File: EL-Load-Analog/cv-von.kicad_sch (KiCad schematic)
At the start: 35 parts, among them Q3 MMBT5551, Q5 MMBT5401, Q6 MMBT5551, U401 AD8038, U402 LM393, U403 74HCT02

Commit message: Working on #4,#2 fixed #8,#22
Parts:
- C401: value 670n -> 680n; Part Name (none) -> C_680nF_25V_X7R_10%_0805
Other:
- note added: "TODO: Select different opamp. TLV2370 (pin compatible)"
- note removed: "TODO: Select different opamp."
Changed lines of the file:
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@@
     (effects (font (size 1.27 1.27)) (justify left bottom))
   )
-  (text "TODO: Select different opamp." (at 108.585 157.48 0)
+  (text "TODO: Select different opamp.\nTLV2370 (pin compatible)\n"
+    (at 108.585 157.48 0)
     (effects (font (size 1.27 1.27)) (justify left bottom))
   )
@@
   (symbol (lib_id "Device:C_Small") (at 102.87 191.135 90) (unit 1)
     (in_bom yes) (on_board yes) (dnp no) (fields_autoplaced)
-    (property "Reference" "C401" (at 102.8763 184.785 90)
-      (effects (font (size 1.27 1.27)))
-    )
-    (property "Value" "670n" (at 102.8763 187.325 90)
+    (property "Reference" "C401" (at 102.8763 184.15 90)
+      (effects (font (size 1.27 1.27)))
+    )
+    (property "Value" "680n" (at 102.8763 186.69 90)
       (effects (font (size 1.27 1.27)))
     )
@@
       (effects (font (size 1.27 1.27)) hide)
     )
+    (property "Part Name" "C_680nF_25V_X7R_10%_0805" (at 102.87 191.135 0)
+      (effects (font (size 1.27 1.27)) hide)
+    )

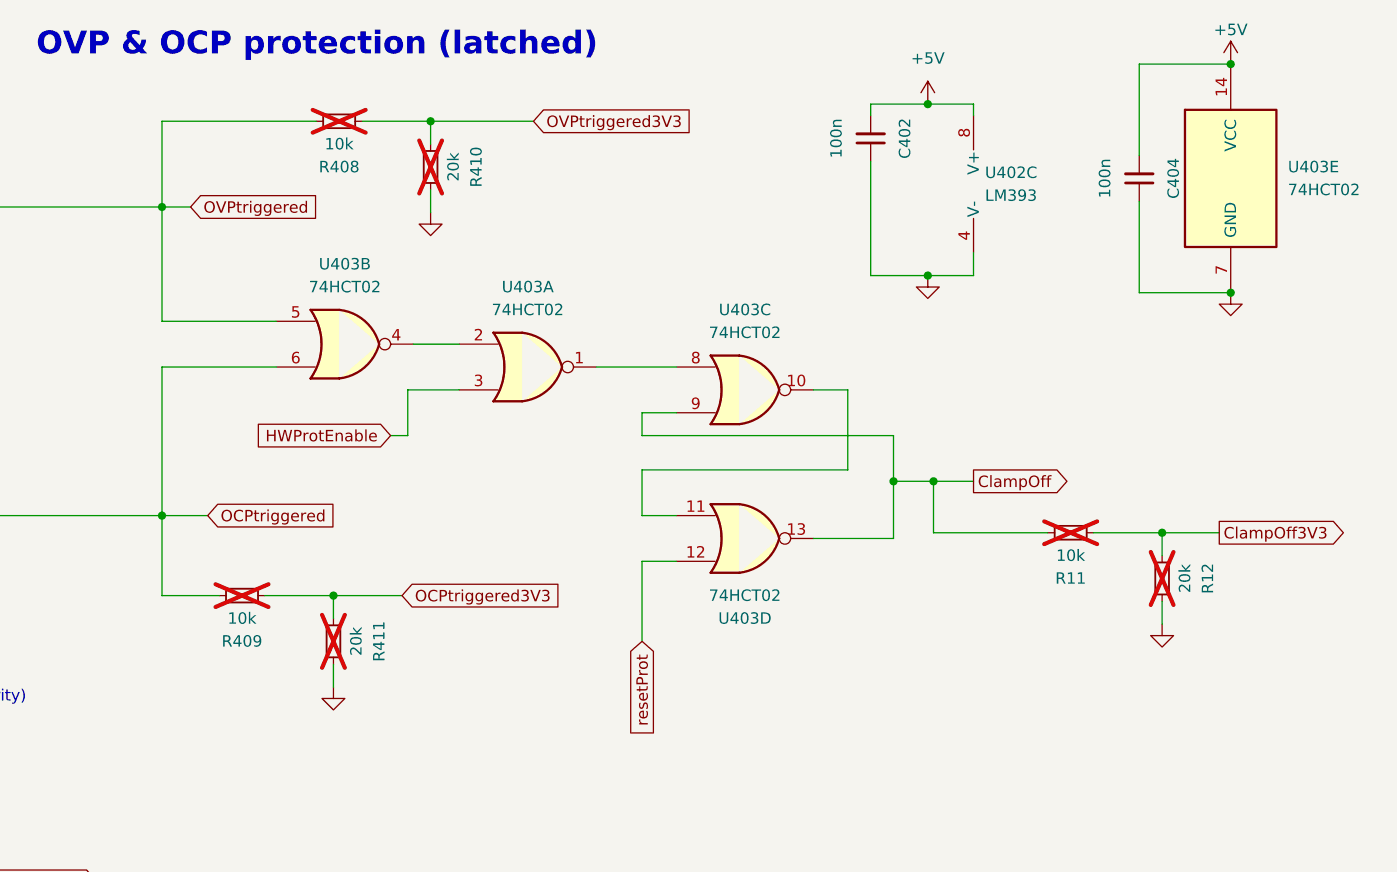
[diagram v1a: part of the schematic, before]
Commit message: Fixing issues from #4, adding ESD protection (#6)
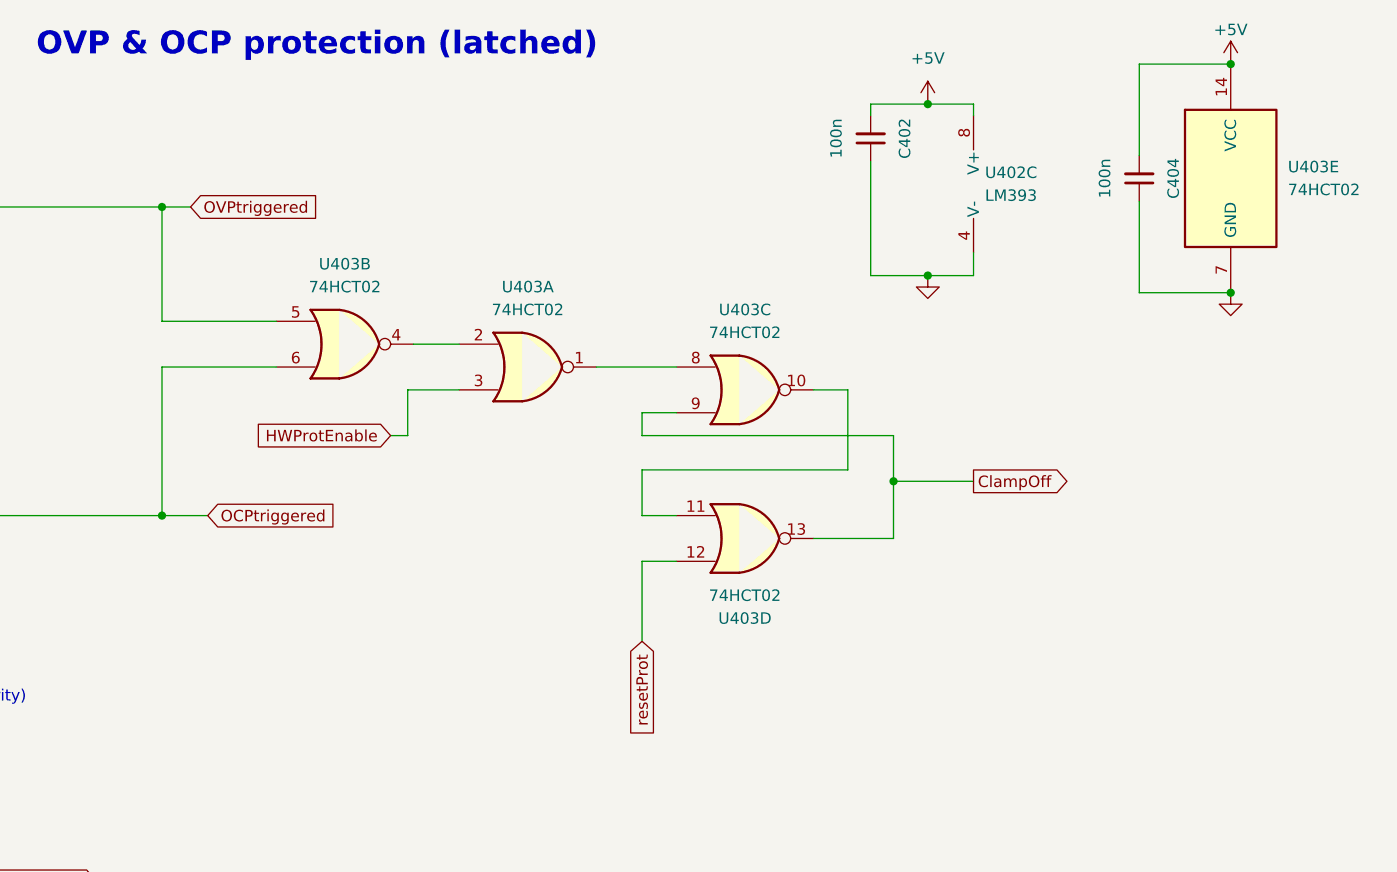
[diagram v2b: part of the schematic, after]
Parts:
- removed R11, R408, R409: 10k, Resistor_SMD:R_0805_2012Metric, symbol Device:R_Small
- removed R12, R410, R411: 20k, Resistor_SMD:R_0805_2012Metric, symbol Device:R_Small

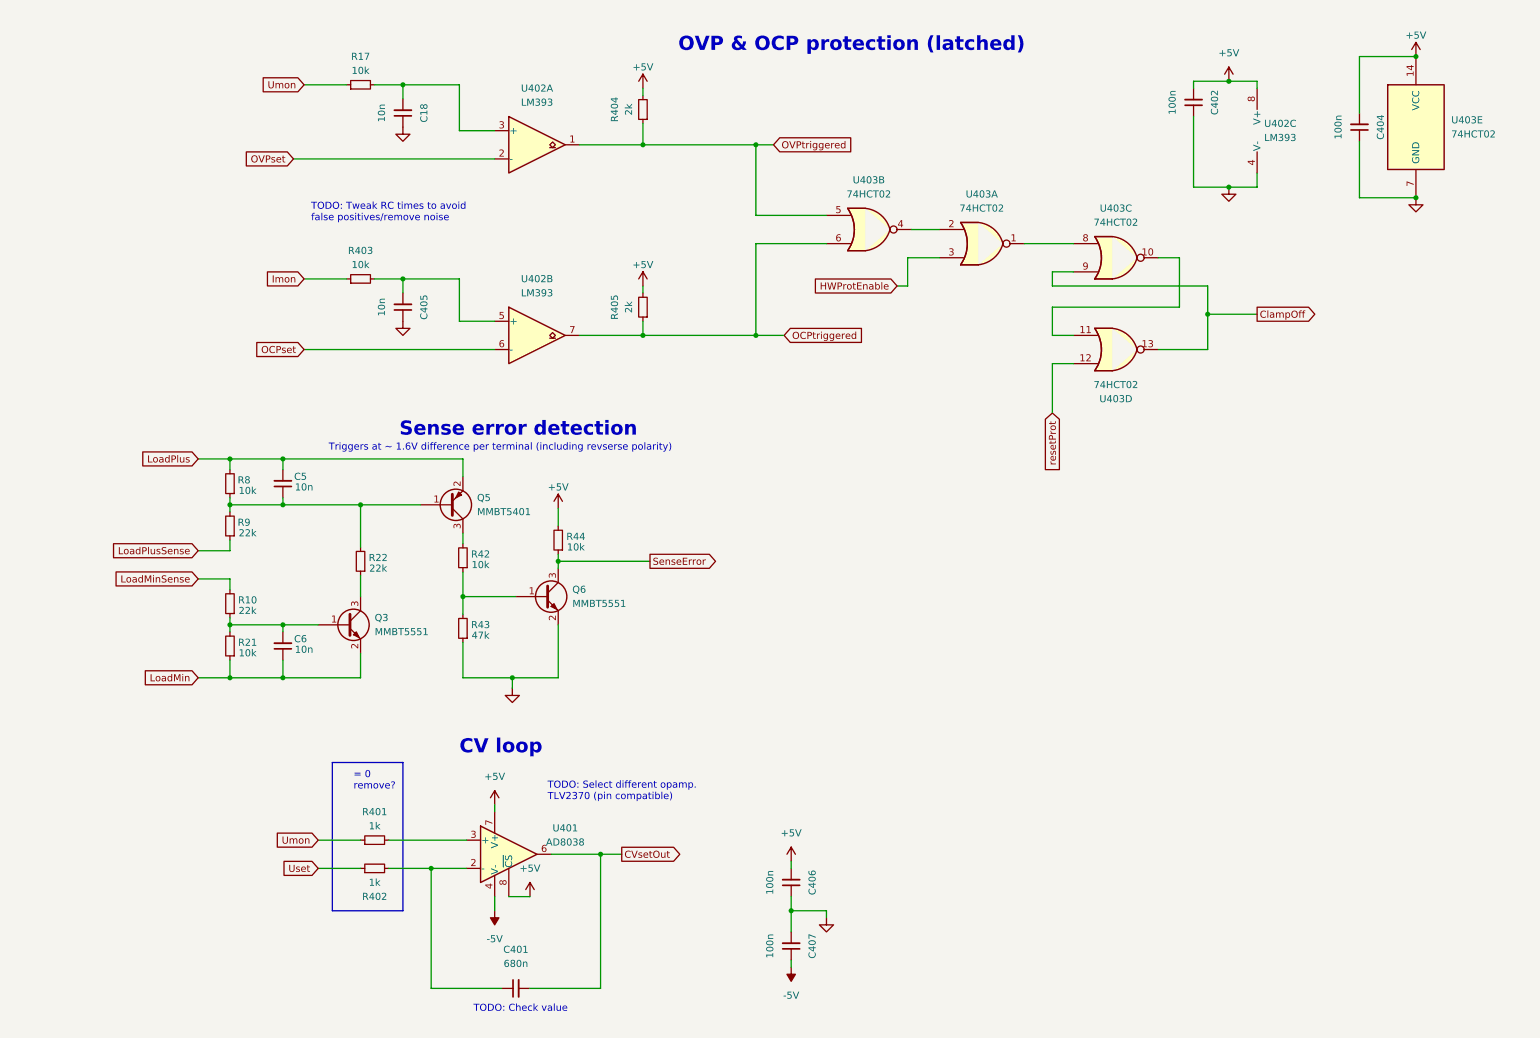
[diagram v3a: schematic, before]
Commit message: v4 Analog board design. Features reverse polarity, remote sense error and new clamping circuitry.
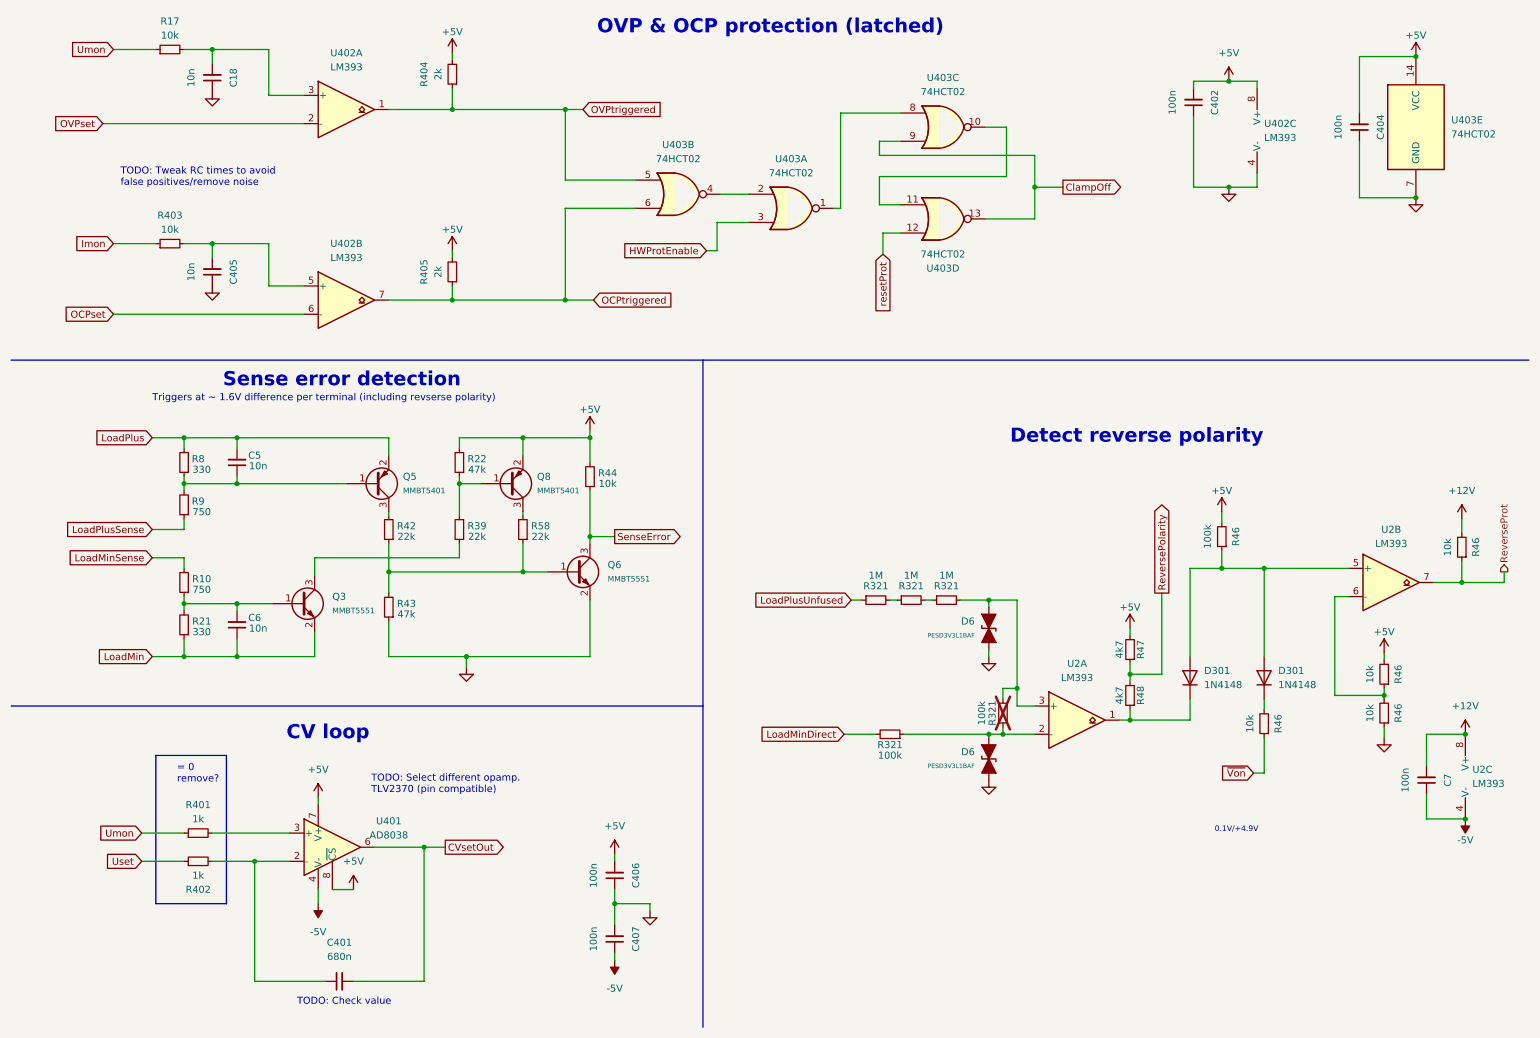
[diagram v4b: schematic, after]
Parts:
- added C7: 100n, Capacitor_SMD:C_0805_2012Metric, symbol Device:C_Small
- added D301 (x2): 1N4148, Diode_SMD:D_MiniMELF, symbol Diode:1N4148
- added D6 (x2): PESD3V3L1BAF, Diode_SMD:D_SOD-323, symbol Device:D_TVS_Filled
- added Q8: MMBT5401, Package_TO_SOT_SMD:SOT-23, symbol EL-Load:MMBT5401
- added R321 (x3): 1M, Resistor_SMD:R_0805_2012Metric, symbol Device:R_Small
- added R321 (x2), R46: 100k, Resistor_SMD:R_0805_2012Metric, symbol Device:R_Small
- added R39, R58: 22k, Resistor_SMD:R_0805_2012Metric, symbol Device:R_Small
- added R46 (x4): 10k, Resistor_SMD:R_0805_2012Metric, symbol Device:R_Small
- added R47, R48: 4k7, Resistor_SMD:R_0805_2012Metric, symbol Device:R_Small
- added U2: LM393, Package_SO:SOIC-8_3.9x4.9mm_P1.27mm, symbol Comparator:LM393
- C402, C404, C406, C407: Part Name C_100.0nF_0805_20% -> C_100.0nF_50V_0805_10%_X7R
- R10, R9: value 22k -> 750; Part Name R_22.0kΩ_0805_1% -> R_750.0Ω_0805_1%
- R21, R8: value 10k -> 330; Part Name R_10.0kΩ_0805_1% -> R_330.0Ω_0805_1%
- R22: value 22k -> 47k; Part Name R_22.0kΩ_0805_1% -> R_47.0kΩ_0805_1%
- R42: value 10k -> 22k; Part Name R_10.0kΩ_0805_1% -> R_22.0kΩ_0805_1%
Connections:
- net +5V: now also R22.2, Q8.2 (E), R46.2, R46.2, R47.2
- net -5V: now also C7.1, U2.4 (V-)
- net GND: now also D6.1 (A1), D6.1 (A1), R46.1
- net at C5.1, Q5.1 (B), R8.1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: no longer R22.2
- net at Q6.1 (B), R42.1, R43.2: now also R58.1
- net at Q3.3 (C): now also R39.1; no longer R22.1
- new net: R46.1, R46.2, U2.6 (-)
- new net: D6.2 (A2), R321.1, R321.1, U2.2 (-)
- new net: Q8.1 (B), R22.1, R39.2
- new net: Q8.3 (C), R58.2
- new net: R321.1, R321.2 (x2)
- new net: D6.2 (A2), R321.2, R321.2, U2.3 (+)
- new net: D301.1 (K), R48.1, U2.1
- new net: D301.2 (A), D301.2 (A), R46.1, U2.5 (+)
- new net: D301.1 (K), R46.2
- new net +12V: C7.2, R46.2, U2.8 (V+)
- new net LoadMinDirect: R321.2
- new net LoadPlusUnfused: R321.1
- new net ReversePolarity: R47.1, R48.2
- new net ReverseProt: R46.1, U2.7
- new net ~{Von}: R46.1
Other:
- note added: "0.1V/+4.9V"
- note added: "Detect reverse polarity"
- moved on the sheet: C18, C401, C405, C406, C407, C5, C6, Q3, Q5, Q6, R10, R17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

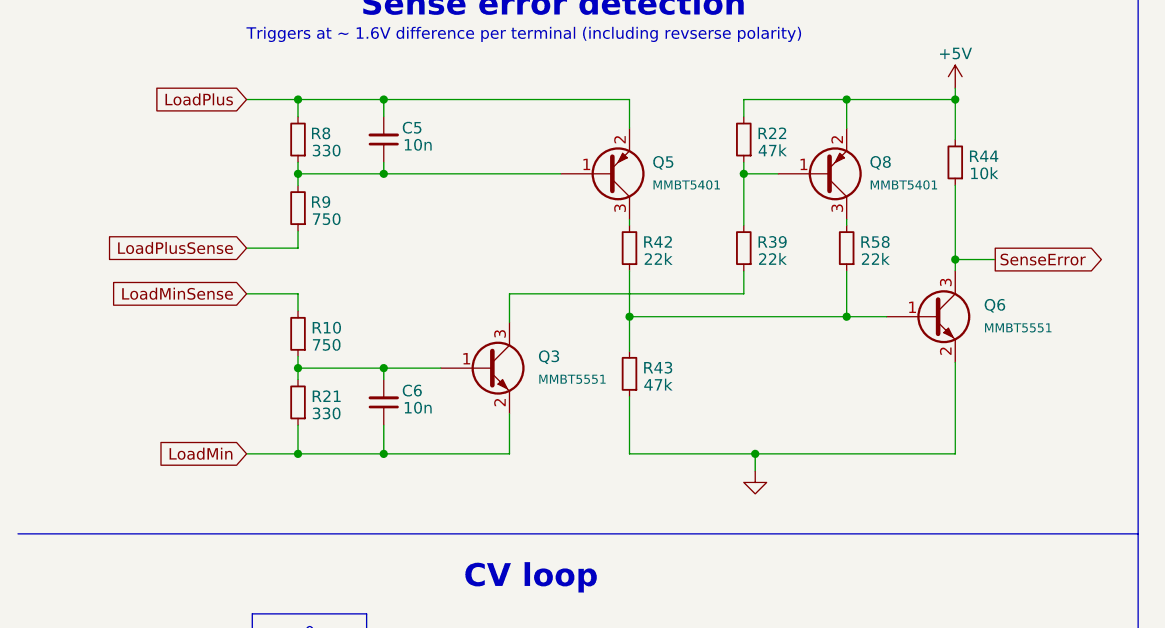
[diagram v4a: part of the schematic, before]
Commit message: Schema changed to 4.1, PCB version E. Modified R44, Remote sense error circtuit had wrong min input.
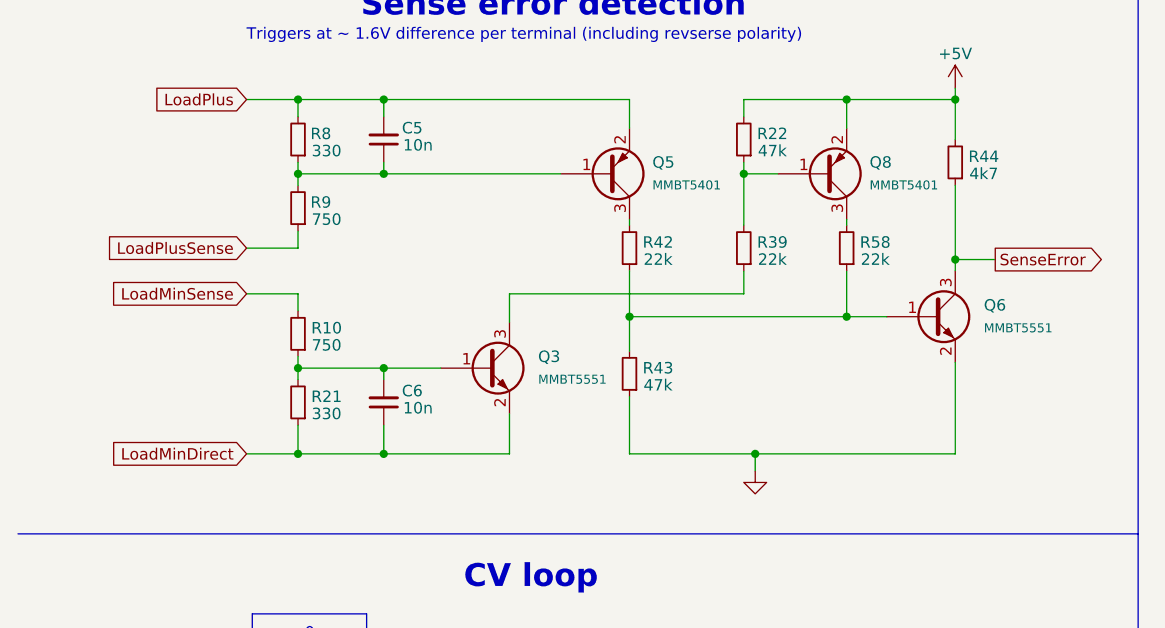
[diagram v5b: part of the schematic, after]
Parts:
- R44: value 10k -> 4k7; Part Name R_10.0kΩ_0805_1% -> R_4.7kΩ_0805_1%
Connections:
- net LoadMin is gone; now on net LoadMinDirect: C6.1, Q3.2 (E), R21.1
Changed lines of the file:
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@@
     (effects (font (size 1.27 1.27)) (justify left bottom))
   )
-  (global_label "LoadMin" (shape input) (at 37.465 131.445 180) (fields_autoplaced)
+  (global_label "LoadMinDirect" (shape input) (at 37.465 131.445 180) (fields_autoplaced)
     (effects (font (size 1.27 1.27)) (justify right))
-    (property "Intersheetrefs" "${INTERSHEET_REFS}" (at 26.7995 131.445 0)
+    (property "Intersheetrefs" "${INTERSHEET_REFS}" (at 21.2356 131.445 0)
       (effects (font (size 1.27 1.27)) (justify right))
     )
@@
       (effects (font (size 1.27 1.27)))
     )
-    (property "Value" "10k" (at 119.38 100.33 0)
+    (property "Value" "4k7" (at 119.38 100.33 0)
       (effects (font (size 1.27 1.27)))
     )
@@
       (effects (font (size 1.27 1.27)) hide)
     )
-    (property "Part Name" "R_10.0kΩ_0805_1%" (at 116.205 99.06 0)
-      (effects (font (size 1.27 1.27)) hide)
-    )
+    (property "Part Name" "R_4.7kΩ_0805_1%" (at 116.205 99.06 0)
+      (effects (font (size 1.27 1.27)) hide)
+    )
